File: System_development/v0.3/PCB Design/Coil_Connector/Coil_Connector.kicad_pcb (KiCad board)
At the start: 2 copper layers, 15.5 x 26.7 mm, 4 parts, among them J1 Conn_Coaxial

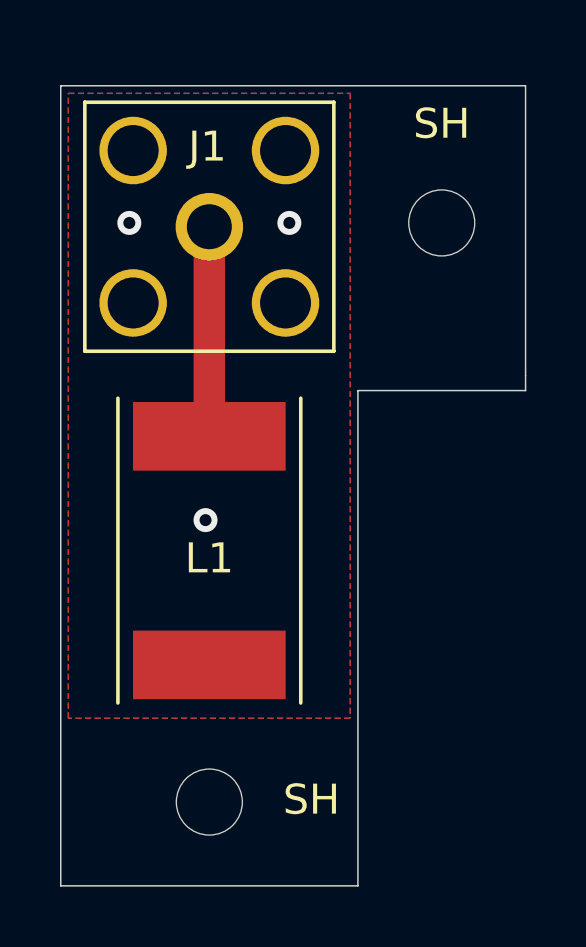
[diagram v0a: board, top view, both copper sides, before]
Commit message: Added V2 of coil pbc and voltage regulation pcb
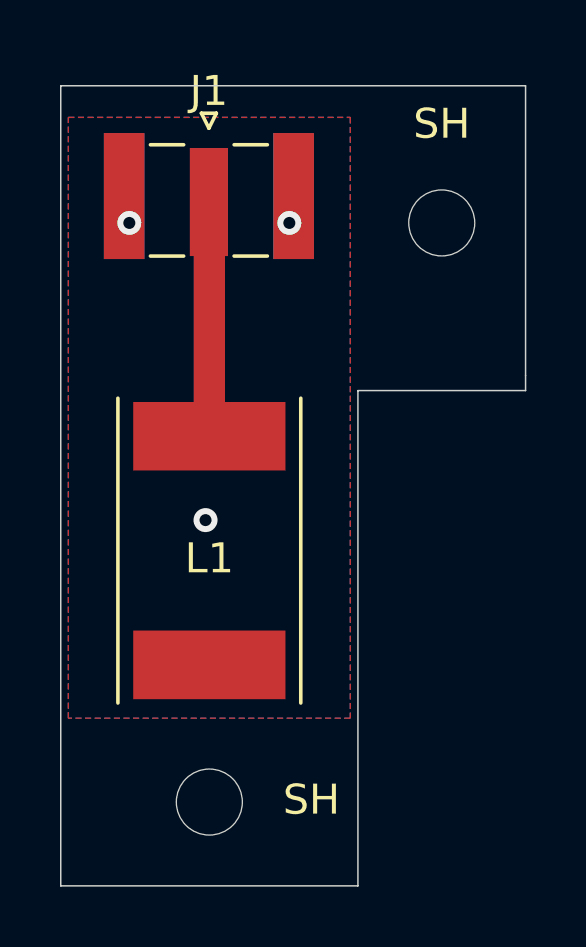
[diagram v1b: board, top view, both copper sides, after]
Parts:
- J1: footprint Connector_Coaxial:SMA_Amphenol_132203-12_Horizontal -> Connector_Coaxial:SMA_Samtec_SMA-J-P-X-ST-EM1_EdgeMount
- moved J1 1.02 mm to (139.1, 100.5)
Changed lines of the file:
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@@
   (net 1 "GND")
   (net 2 "Net-(J1-Pad1)")
-  (footprint "Connector_Coaxial:SMA_Amphenol_132203-12_Horizontal" (layer "F.Cu")
-    (at 139.065 101.473)
-    (descr "https://www.amphenolrf.com/media/downloads/1769/132203-12.pdf")
-    (tags "SMA THT Female Jack Horizontal")
-    (attr through_hole)
-    (fp_text reference "J1" (at -0.0635 -2.667 180) (layer "F.SilkS")
+  (footprint "Connector_Coaxial:SMA_Samtec_SMA-J-P-X-ST-EM1_EdgeMount" (layer "F.Cu")
+    (at 139.05 100.45)
+    (descr "Connector SMA, 0Hz to 20GHz, 50Ohm, Edge Mount (http://suddendocs.samtec.com/prints/sma-j-p-x-st-em1-mkt.pdf)")
+    (tags "SMA Straight Samtec Edge Mount")
+    (attr smd)
+    (fp_text reference "J1" (at 0 -3.5) (layer "F.SilkS")
       (effects (font (size 1 1) (thickness 0.15)))
     )
-    (fp_text value "Conn_Coaxial" (at 0 5) (layer "F.Fab")
+    (fp_text value "Conn_Coaxial" (at 0 13) (layer "F.Fab")
       (effects (font (size 1 1) (thickness 0.15)))
     )
-    (fp_text user "${REFERENCE}" (at 0 0) (layer "F.Fab")
+    (fp_text user "PCB Edge" (at 0 2.6) (layer "Dwgs.User")
+      (effects (font (size 0.5 0.5) (thickness 0.1)))
+    )
+    (fp_text user "Board Thickness: 1.57mm" (at 0 -5.45) (layer "Cmts.User")
       (effects (font (size 1 1) (thickness 0.15)))
     )
-    (fp_line (start 4.15 -4.15) (end 4.15 4.15) (layer "F.SilkS") (width 0.12))
-    (fp_line (start -4.15 -4.15) (end -4.15 4.15) (layer "F.SilkS") (width 0.12))
-    (fp_line (start -4.15 -4.15) (end 4.15 -4.15) (layer "F.SilkS") (width 0.12))
-    (fp_line (start -4.15 4.15) (end 4.15 4.15) (layer "F.SilkS") (width 0.12))
-    (fp_line (start 4.5 4.5) (end 4.5 -20) (layer "F.CrtYd") (width 0.05))
-    (fp_line (start -4.5 -20) (end 4.5 -20) (layer "F.CrtYd") (width 0.05))
-    (fp_line (start 4.5 4.5) (end -4.5 4.5) (layer "F.CrtYd") (width 0.05))
-    (fp_line (start -4.5 -20) (end -4.5 4.5) (layer "F.CrtYd") (width 0.05))
-    (fp_line (start -3.175 -16.588) (end 3.175 -17.294) (layer "F.Fab") (width 0.1))
-    (fp_line (start -3.175 -8.116) (end 3.175 -8.822) (layer "F.Fab") (width 0.1))
-    (fp_line (start -3.175 -10.234) (end 3.175 -10.94) (layer "F.Fab") (width 0.1))
-    (fp_line (start -3.175 -18) (end 3.175 -18.706) (layer "F.Fab") (width 0.1))
-    (fp_line (start 3.175 -19.5) (end 3.175 -5.07) (layer "F.Fab") (width 0.1))
-    (fp_line (start -3.175 -11.646) (end 3.175 -12.352) (layer "F.Fab") (width 0.1))
-    (fp_line (start -4 -4) (end 4 -4) (layer "F.Fab") (width 0.1))
-    (fp_line (start -3.175 -8.822) (end 3.175 -9.528) (layer "F.Fab") (width 0.1))
-    (fp_line (start 3.9 -5.07) (end -3.9 -5.07) (layer "F.Fab") (width 0.1))
-    (fp_line (start -3.175 -13.058) (end 3.175 -13.764) (layer "F.Fab") (width 0.1))
-    (fp_line (start 4 -4) (end 4 4) (layer "F.Fab") (width 0.1))
-    (fp_line (start 3.9 -4) (end 3.9 -5.07) (layer "F.Fab") (width 0.1))
-    (fp_line (start -3.175 -17.294) (end 3.175 -18) (layer "F.Fab") (width 0.1))
-    (fp_line (start -3.175 -6.704) (end 3.175 -7.41) (layer "F.Fab") (width 0.1))
-    (fp_line (start -3.175 -14.47) (end 3.175 -15.176) (layer "F.Fab") (width 0.1))
-    (fp_line (start -3.175 -7.41) (end 3.175 -8.116) (layer "F.Fab") (width 0.1))
-    (fp_line (start -3.175 -13.764) (end 3.175 -14.47) (layer "F.Fab") (width 0.1))
-    (fp_line (start -4 4) (end 4 4) (layer "F.Fab") (width 0.1))
-    (fp_line (start -3.175 -15.882) (end 3.175 -16.588) (layer "F.Fab") (width 0.1))
-    (fp_line (start -4 -4) (end -4 4) (layer "F.Fab") (width 0.1))
-    (fp_line (start -3.175 -19.5) (end 3.175 -19.5) (layer "F.Fab") (width 0.1))
-    (fp_line (start -3.175 -9.528) (end 3.175 -10.234) (layer "F.Fab") (width 0.1))
-    (fp_line (start -3.175 -10.94) (end 3.175 -11.646) (layer "F.Fab") (width 0.1))
-    (fp_line (start -3.175 -5.998) (end 3.175 -6.704) (layer "F.Fab") (width 0.1))
-    (fp_line (start -3.175 -12.352) (end 3.175 -13.058) (layer "F.Fab") (width 0.1))
-    (fp_line (start -3.175 -15.176) (end 3.175 -15.882) (layer "F.Fab") (width 0.1))
-    (fp_line (start -3.9 -5.07) (end -3.9 -4) (layer "F.Fab") (width 0.1))
-    (fp_line (start -3.175 -19.5) (end -3.175 -5.07) (layer "F.Fab") (width 0.1))
-    (pad "1" thru_hole circle locked (at 0 0) (size 2.25 2.25) (drill 1.5) (layers *.Cu *.Mask)
+    (fp_text user "${REFERENCE}" (at 0 4.79) (layer "F.Fab")
+      (effects (font (size 1 1) (thickness 0.15)))
+    )
+    (fp_line (start 0.25 -2.76) (end -0.25 -2.76) (layer "F.SilkS") (width 0.12))
+    (fp_line (start -1.95 -1.71) (end -0.84 -1.71) (layer "F.SilkS") (width 0.12))
+    (fp_line (start -1.95 2) (end -0.84 2) (layer "F.SilkS") (width 0.12))
+    (fp_line (start 0 -2.26) (end 0.25 -2.76) (layer "F.SilkS") (width 0.12))
+    (fp_line (start -0.25 -2.76) (end 0 -2.26) (layer "F.SilkS") (width 0.12))
+    (fp_line (start 0.84 -1.71) (end 1.95 -1.71) (layer "F.SilkS") (width 0.12))
+    (fp_line (start 0.84 2) (end 1.95 2) (layer "F.SilkS") (width 0.12))
+    (fp_line (start 4.1 2.1) (end -4.1 2.1) (layer "Dwgs.User") (width 0.1))
+    (fp_line (start -3.68 2.6) (end -4 2.6) (layer "B.CrtYd") (width 0.05))
+    (fp_line (start -3.68 12.12) (end -3.68 2.6) (layer "B.CrtYd") (width 0.05))
+    (fp_line (start 4 2.6) (end 4 -2.6) (layer "B.CrtYd") (width 0.05))
+    (fp_line (start -4 2.6) (end -4 -2.6) (layer "B.CrtYd") (width 0.05))
+    (fp_line (start 3.68 2.6) (end 3.68 12.12) (layer "B.CrtYd") (width 0.05))
+    (fp_line (start -4 -2.6) (end 4 -2.6) (layer "B.CrtYd") (width 0.05))
+    (fp_line (start 4 2.6) (end 3.68 2.6) (layer "B.CrtYd") (width 0.05))
+    (fp_line (start 3.68 12.12) (end -3.68 12.12) (layer "B.CrtYd") (width 0.05))
+    (fp_line (start -4 -2.6) (end 4 -2.6) (layer "F.CrtYd") (width 0.05))
+    (fp_line (start -3.68 12.12) (end -3.68 2.6) (layer "F.CrtYd") (width 0.05))
+    (fp_line (start 3.68 12.12) (end -3.68 12.12) (layer "F.CrtYd") (width 0.05))
+    (fp_line (start 4 2.6) (end 4 -2.6) (layer "F.CrtYd") (width 0.05))
+    (fp_line (start 3.68 2.6) (end 4 2.6) (layer "F.CrtYd") (width 0.05))
+    (fp_line (start -4 2.6) (end -4 -2.6) (layer "F.CrtYd") (width 0.05))
+    (fp_line (start -3.68 2.6) (end -4 2.6) (layer "F.CrtYd") (width 0.05))
+    (fp_line (start 3.68 2.6) (end 3.68 12.12) (layer "F.CrtYd") (width 0.05))
+    (fp_line (start 3.175 -1.71) (end 2.365 -1.71) (layer "F.Fab") (width 0.1))
+    (fp_line (start 2.365 2.1) (end -2.365 2.1) (layer "F.Fab") (width 0.1))
+    (fp_line (start -2.365 -1.71) (end -3.175 -1.71) (layer "F.Fab") (width 0.1))
+    (fp_line (start -3.175 -1.71) (end -3.175 11.62) (layer "F.Fab") (width 0.1))
+    (fp_line (start 0 3.1) (end -0.64 2.1) (layer "F.Fab") (width 0.1))
+    (fp_line (start 3.175 -1.71) (end 3.175 11.62) (layer "F.Fab") (width 0.1))
+    (fp_line (start 3.165 11.62) (end -3.165 11.62) (layer "F.Fab") (width 0.1))
+    (fp_line (start 0.64 2.1) (end 0 3.1) (layer "F.Fab") (width 0.1))
+    (fp_line (start -2.365 2.1) (end -2.365 -1.71) (layer "F.Fab") (width 0.1))
+    (fp_line (start 2.365 -1.71) (end 2.365 2.1) (layer "F.Fab") (width 0.1))
+    (pad "1" smd rect (at 0 0.2) (size 1.27 3.6) (layers "F.Cu" "F.Paste" "F.Mask")
       (net 2 "Net-(J1-Pad1)"))
-    (pad "2" thru_hole circle locked (at -2.54 -2.54) (size 2.25 2.25) (drill 1.7) (layers *.Cu *.Mask)
+    (pad "2" smd rect (at 2.825 0) (size 1.35 4.2) (layers "B.Cu" "B.Paste" "B.Mask")
       (net 1 "GND"))
-    (pad "2" thru_hole circle locked (at 2.54 2.54 90) (size 2.25 2.25) (drill 1.7) (layers *.Cu *.Mask)
+    (pad "2" smd rect (at 2.825 0) (size 1.35 4.2) (layers "F.Cu" "F.Paste" "F.Mask")
       (net 1 "GND"))
-    (pad "2" thru_hole circle locked (at -2.54 2.54) (size 2.25 2.25) (drill 1.7) (layers *.Cu *.Mask)
+    (pad "2" smd rect (at -2.825 0) (size 1.35 4.2) (layers "B.Cu" "B.Paste" "B.Mask")
       (net 1 "GND"))
-    (pad "2" thru_hole circle locked (at 2.54 -2.54) (size 2.25 2.25) (drill 1.7) (layers *.Cu *.Mask)
+    (pad "2" smd rect (at -2.825 0) (size 1.35 4.2) (layers "F.Cu" "F.Paste" "F.Mask")
       (net 1 "GND"))
-    (model "${KISYS3DMOD}/Connector_Coaxial.3dshapes/SMA_Amphenol_132203-12_Horizontal.wrl"
+    (model "${KICAD6_3DMODEL_DIR}/Connector_Coaxial.3dshapes/SMA_Samtec_SMA-J-P-X-ST-EM1_EdgeMount.wrl"
       (offset (xyz 0 0 0))
       (scale (xyz 1 1 1))
@@
     (connect_pads (clearance 0.508))
     (min_thickness 0.254) (filled_areas_thickness no)
-    (fill yes (thermal_gap 0.508) (thermal_bridge_width 0.508))
+    (fill (thermal_gap 0.508) (thermal_bridge_width 0.508))
     (polygon
       (pts
         (xy 143.764 117.856)
         (xy 134.366 117.856)
-        (xy 134.366 97.028)
-        (xy 143.764 97.028)
+        (xy 134.366 97.828)
+        (xy 143.764 97.828)
       )
     )
@@
     (connect_pads (clearance 0.508))
     (min_thickness 0.254) (filled_areas_thickness no)
-    (fill yes (thermal_gap 0.508) (thermal_bridge_width 0.508))
+    (fill (thermal_gap 0.508) (thermal_bridge_width 0.508))
     (polygon
       (pts
         (xy 143.764 117.856)
         (xy 134.366 117.856)
-        (xy 134.366 97.028)
-        (xy 143.764 97.028)
+        (xy 134.366 97.828)
+        (xy 143.764 97.828)
       )
     )
